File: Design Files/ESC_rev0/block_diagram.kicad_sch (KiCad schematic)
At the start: 0 parts

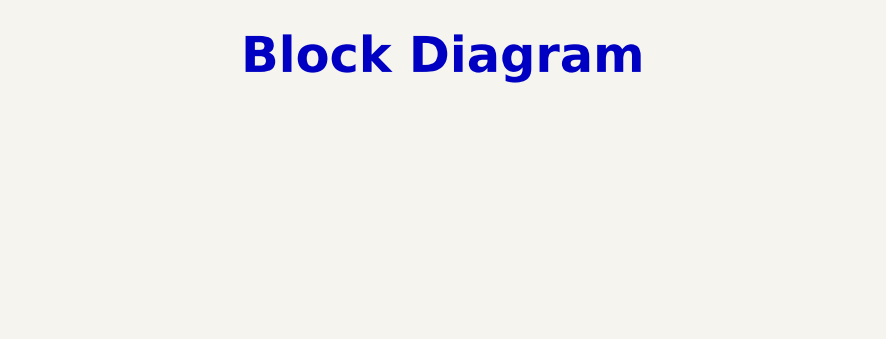
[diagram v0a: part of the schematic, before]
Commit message: update10
modifications to root page, completion of pages step_down and mechanical
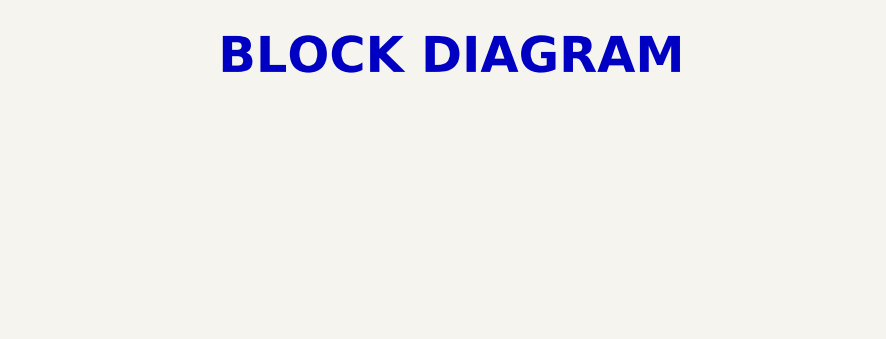
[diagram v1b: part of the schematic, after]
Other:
- title: Block Diagram ->  BLOCK DIAGRAM
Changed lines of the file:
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@@
 	(paper "A4")
 	(title_block
-		(title "Block Diagram")
+		(title " BLOCK DIAGRAM")
 		(rev "0")
 	)

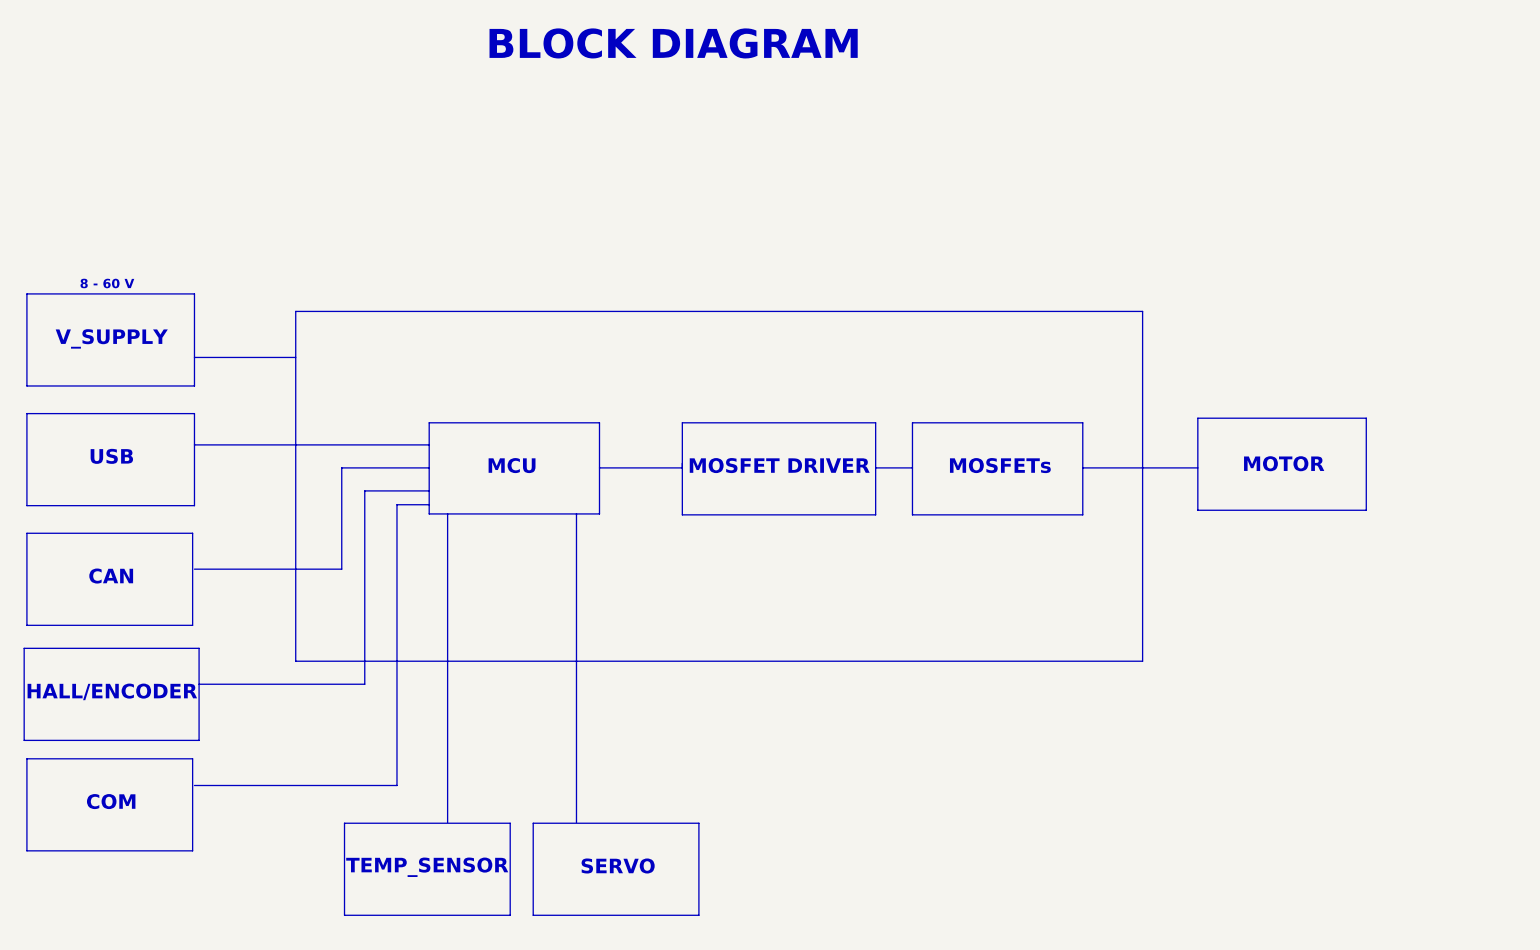
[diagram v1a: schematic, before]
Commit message: UPDATE 12
started schematics revision: edit and added info and circuits to some pages and assigned some footprints for components
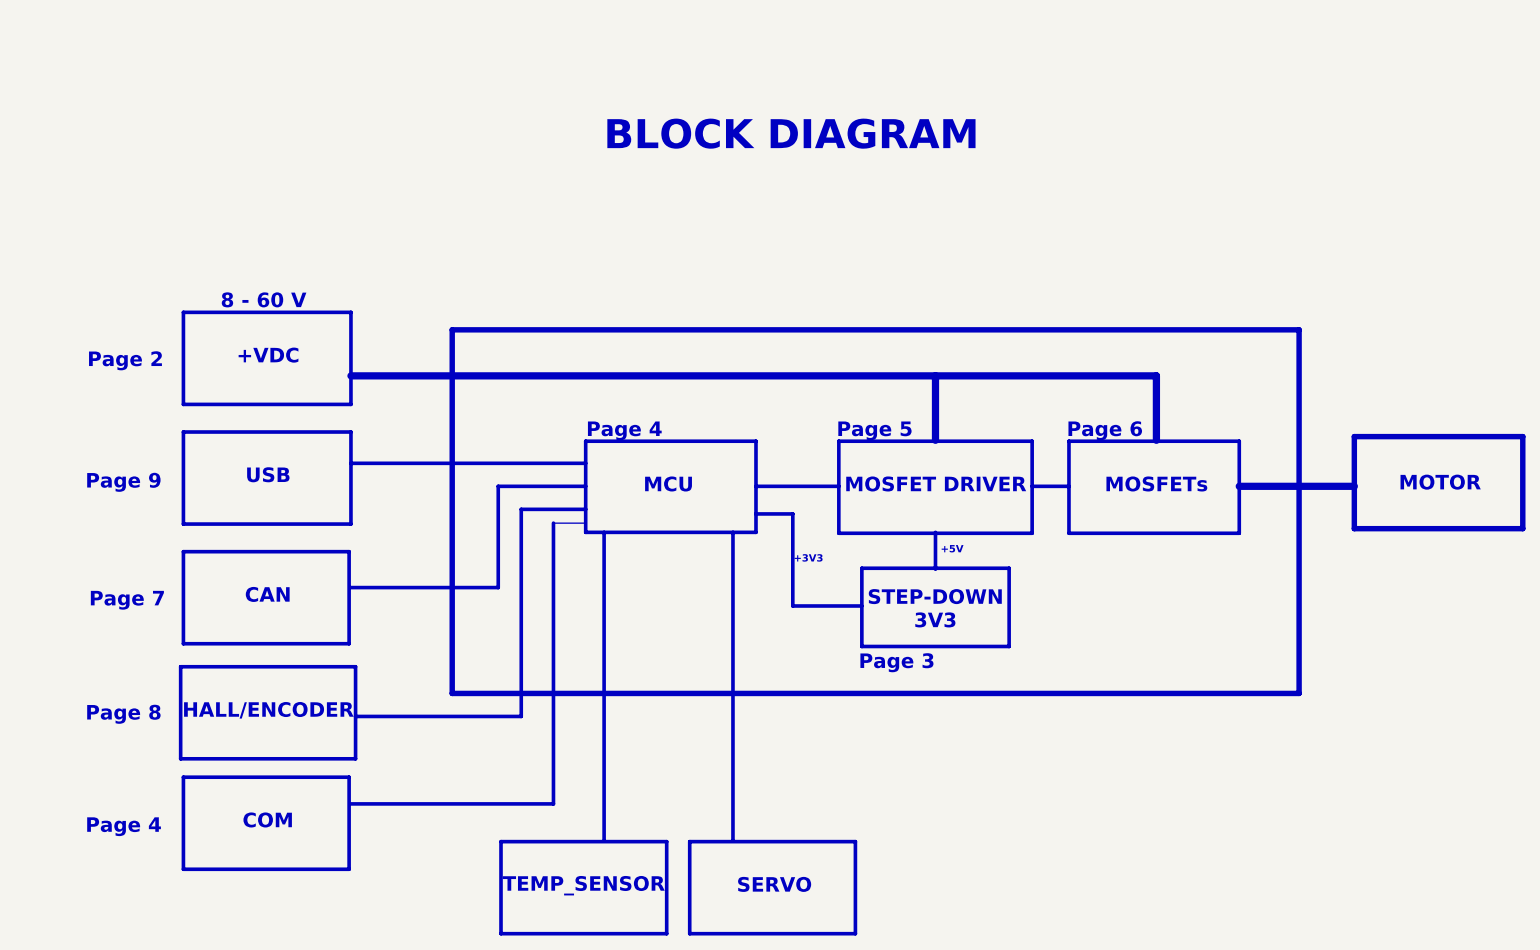
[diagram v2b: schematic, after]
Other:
- note added: "+3V3"
- note added: "+5V"
- note added: "+VDC"
- note added: "Page 2"
- note added: "Page 3"
- note added: "Page 4"
- note added: "Page 5"
- note added: "Page 6"
- note added: "Page 7"
- note added: "Page 8"
- note added: "Page 9"
- note added: "STEP-DOWN 3V3"
- note removed: "V_SUPPLY"
